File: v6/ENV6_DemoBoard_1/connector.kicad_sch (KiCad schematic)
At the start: 1 part, among them J3 Conn_02x12_Odd_Even

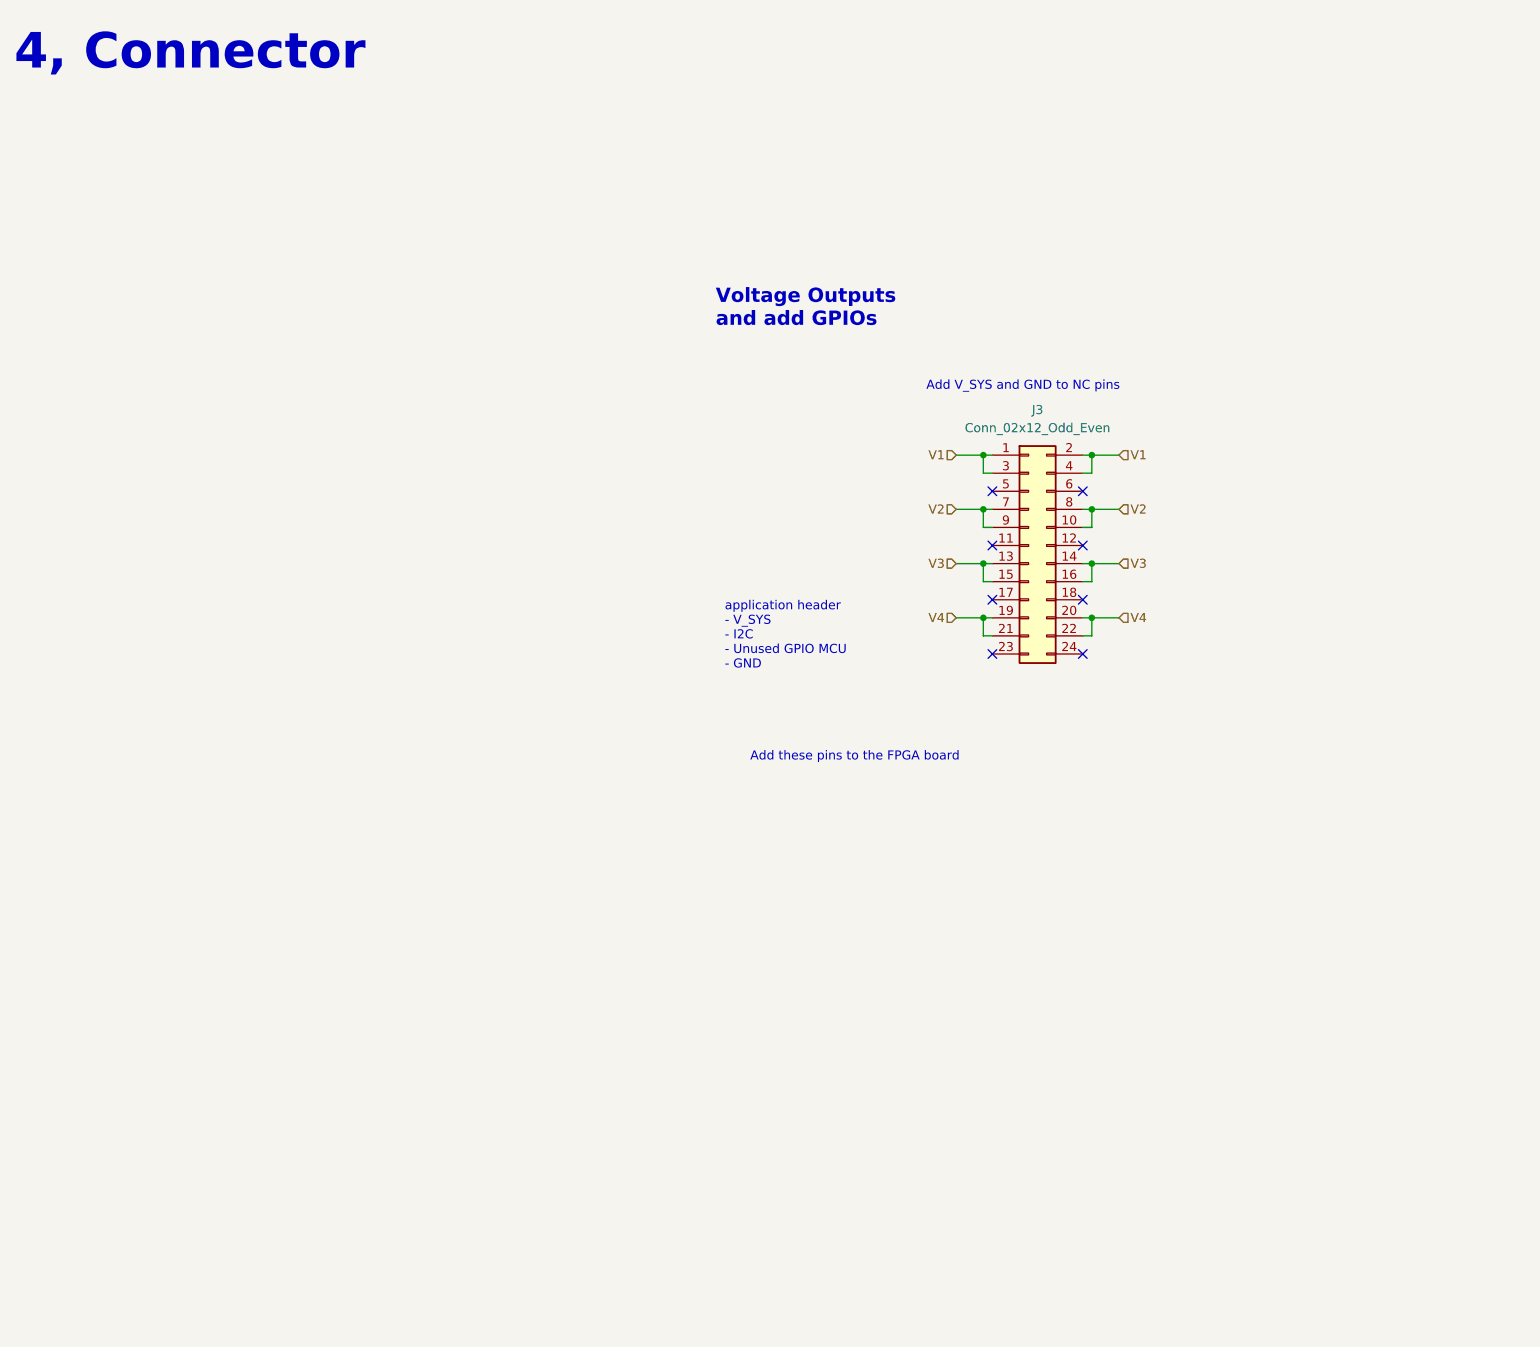
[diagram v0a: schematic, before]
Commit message: update Demoboard and add GateMateA11 board
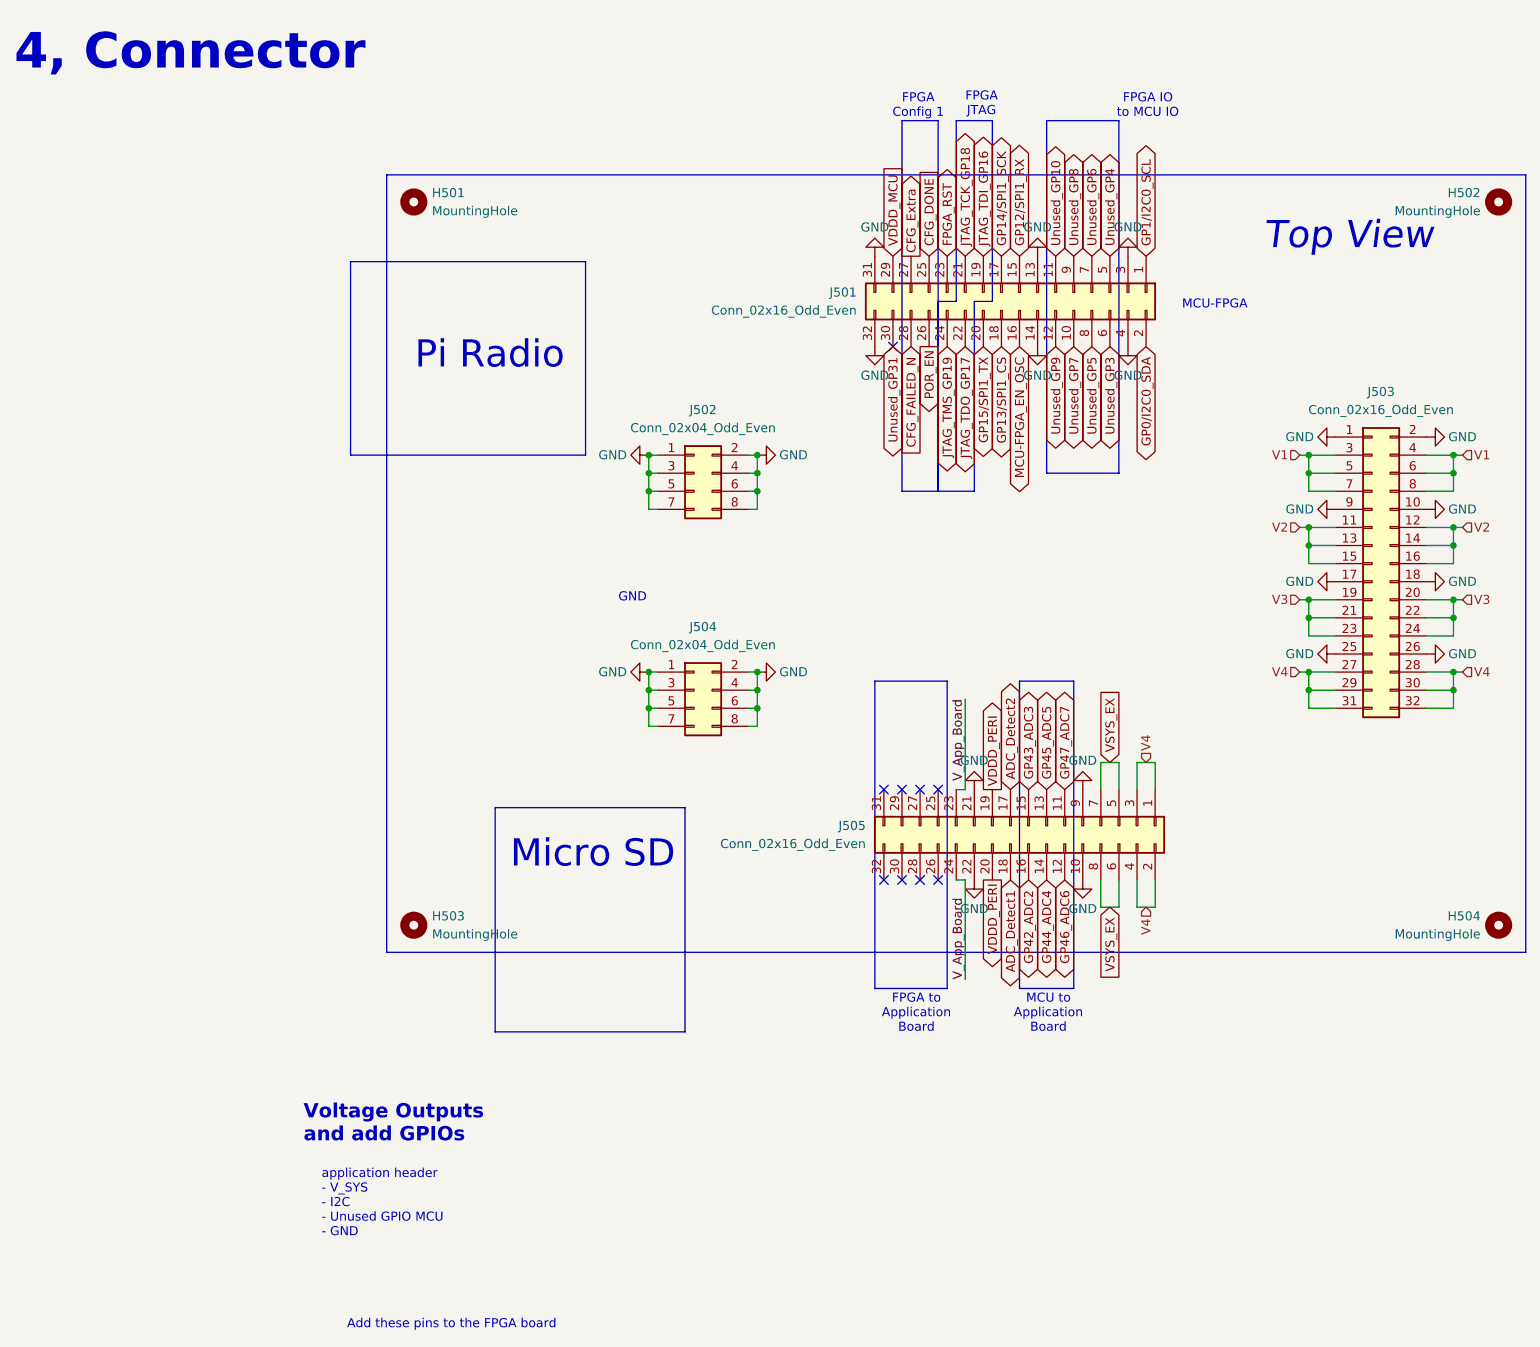
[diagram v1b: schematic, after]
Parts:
- removed J3: Conn_02x12_Odd_Even, Connector_PinSocket_2.54mm:PinSocket_2x12_P2.54mm_Vertical, symbol Connector_Generic:Conn_02x12_Odd_Even
- added H501, H502, H503, H504: MountingHole, MountingHole:MountingHole_2.5mm, symbol Mechanical:MountingHole
- added J501, J503, J505: Conn_02x16_Odd_Even, Connector_PinHeader_2.00mm:PinHeader_2x16_P2.00mm_Vertical, symbol Connector_Generic:Conn_02x16_Odd_Even
- added J502, J504: Conn_02x04_Odd_Even, Connector_PinHeader_2.00mm:PinHeader_2x04_P2.00mm_Vertical, symbol Connector_Generic:Conn_02x04_Odd_Even
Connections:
- net V1: now also J503.3 (Pin_3), J503.4 (Pin_4), J503.5 (Pin_5), J503.6 (Pin_6), J503.7 (Pin_7), J503.8 (Pin_8)
- net V2: now also J503.11 (Pin_11), J503.12 (Pin_12), J503.13 (Pin_13), J503.14 (Pin_14), J503.15 (Pin_15), J503.16 (Pin_16)
- net V3: now also J503.19 (Pin_19), J503.20 (Pin_20), J503.21 (Pin_21), J503.22 (Pin_22), J503.23 (Pin_23), J503.24 (Pin_24)
- net V4: now also J503.27 (Pin_27), J503.28 (Pin_28), J503.29 (Pin_29), J503.30 (Pin_30), J503.31 (Pin_31), J503.32 (Pin_32), J505.1 (Pin_1), J505.2 (Pin_2), J505.3 (Pin_3), J505.4 (Pin_4)
- new net ADC_Detect1: J505.18 (Pin_18)
- new net ADC_Detect2: J505.17 (Pin_17)
- new net CFG_DONE: J501.25 (Pin_25)
- new net CFG_Extra: J501.27 (Pin_27)
- new net CFG_FAILED_N: J501.28 (Pin_28)
- new net FPGA_RST: J501.23 (Pin_23)
- new net GND: J501.13 (Pin_13), J501.14 (Pin_14), J501.3 (Pin_3), J501.31 (Pin_31), J501.32 (Pin_32), J501.4 (Pin_4), J502.1 (Pin_1), J502.2 (Pin_2), J502.3 (Pin_3), J502.4 (Pin_4), J502.5 (Pin_5), J502.6 (Pin_6), J502.7 (Pin_7), J502.8 (Pin_8), J503.1 (Pin_1), J503.10 (Pin_10), J503.17 (Pin_17), J503.18 (Pin_18), J503.2 (Pin_2), J503.25 (Pin_25), J503.26 (Pin_26), J503.9 (Pin_9), J504.1 (Pin_1), J504.2 (Pin_2), J504.3 (Pin_3), J504.4 (Pin_4), J504.5 (Pin_5), J504.6 (Pin_6), J504.7 (Pin_7), J504.8 (Pin_8), J505.10 (Pin_10), J505.21 (Pin_21), J505.22 (Pin_22), J505.9 (Pin_9)
- new net GP0/I2C0_SDA: J501.2 (Pin_2)
- new net GP12/SPI1_RX: J501.15 (Pin_15)
- new net GP13/SPI1_CS: J501.18 (Pin_18)
- new net GP14/SPI1_SCK: J501.17 (Pin_17)
- new net GP15/SPI1_TX: J501.20 (Pin_20)
- new net GP1/I2C0_SCL: J501.1 (Pin_1)
- new net GP42_ADC2: J505.16 (Pin_16)
- new net GP43_ADC3: J505.15 (Pin_15)
- new net GP44_ADC4: J505.14 (Pin_14)
- new net GP45_ADC5: J505.13 (Pin_13)
- new net GP46_ADC6: J505.12 (Pin_12)
- new net GP47_ADC7: J505.11 (Pin_11)
- new net JTAG_TCK_GP18: J501.21 (Pin_21)
- new net JTAG_TDI_GP16: J501.19 (Pin_19)
- new net JTAG_TDO_GP17: J501.22 (Pin_22)
- new net JTAG_TMS_GP19: J501.24 (Pin_24)
- new net MCU-FPGA_EN_OSC: J501.16 (Pin_16)
- new net POR_EN: J501.26 (Pin_26)
- new net Unused_GP10: J501.11 (Pin_11)
- new net Unused_GP3: J501.6 (Pin_6)
- new net Unused_GP31: J501.30 (Pin_30)
- new net Unused_GP4: J501.5 (Pin_5)
- new net Unused_GP5: J501.8 (Pin_8)
- new net Unused_GP6: J501.7 (Pin_7)
- new net Unused_GP7: J501.10 (Pin_10)
- new net Unused_GP8: J501.9 (Pin_9)
- new net Unused_GP9: J501.12 (Pin_12)
- new net VDDD_MCU: J501.29 (Pin_29)
- new net VDDD_PERI: J505.19 (Pin_19), J505.20 (Pin_20)
- new net VSYS_EX: J505.5 (Pin_5), J505.6 (Pin_6), J505.7 (Pin_7), J505.8 (Pin_8)
- new net V_App_Board: J505.23 (Pin_23), J505.24 (Pin_24)
- no-connect marks 8 -> 9
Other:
- note added: "FPGA Config 1"
- note added: "FPGA IO to MCU IO"
- note added: "FPGA JTAG"
- note added: "FPGA to Application Board"
- note added: "GND"
- note added: "MCU to Application Board"
- note added: "MCU-FPGA"
- note added: "Micro SD"
- note added: "Pi Radio"
- note added: "Top View"
- note removed: "Add V_SYS and GND to NC pins"
